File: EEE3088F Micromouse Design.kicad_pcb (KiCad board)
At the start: 2 copper layers, 74.5 x 78.2 mm, 62 parts, among them J1 Conn_02x16_Odd_Even, J2 Conn_01x02, Q2 AO3400A, U1 INA219AxD, U11 DRV8833PW, U12 DRV8833PW, U13 AP22966DC8-7, U15 TP4056-42-ESOP8, U6 TPS5430DDA, U9 CH224K

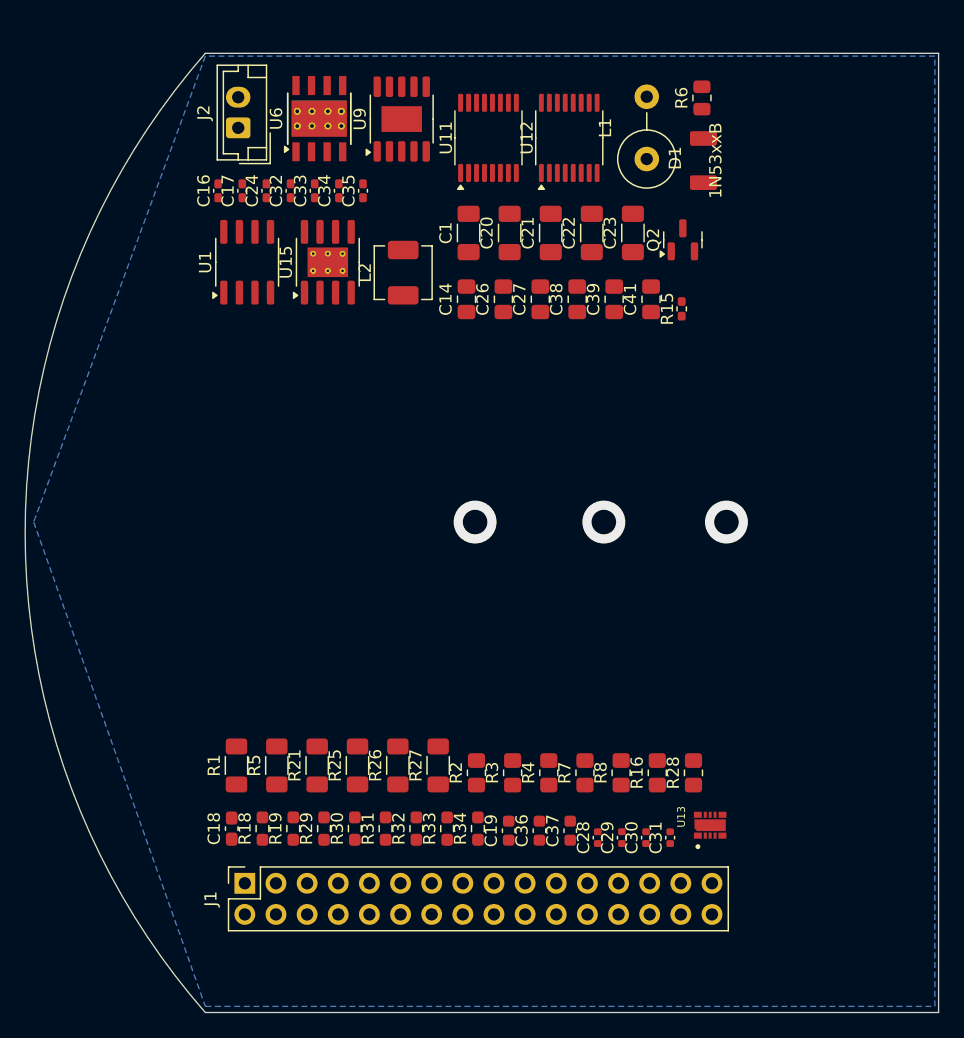
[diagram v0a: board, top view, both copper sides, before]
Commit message: Please Read: Replaced buck converter, removed old ones but this has left behind a gap in the copper. The board also needs a curved arc according to Justin. Still need footprints for key ICs, connectors and my switch
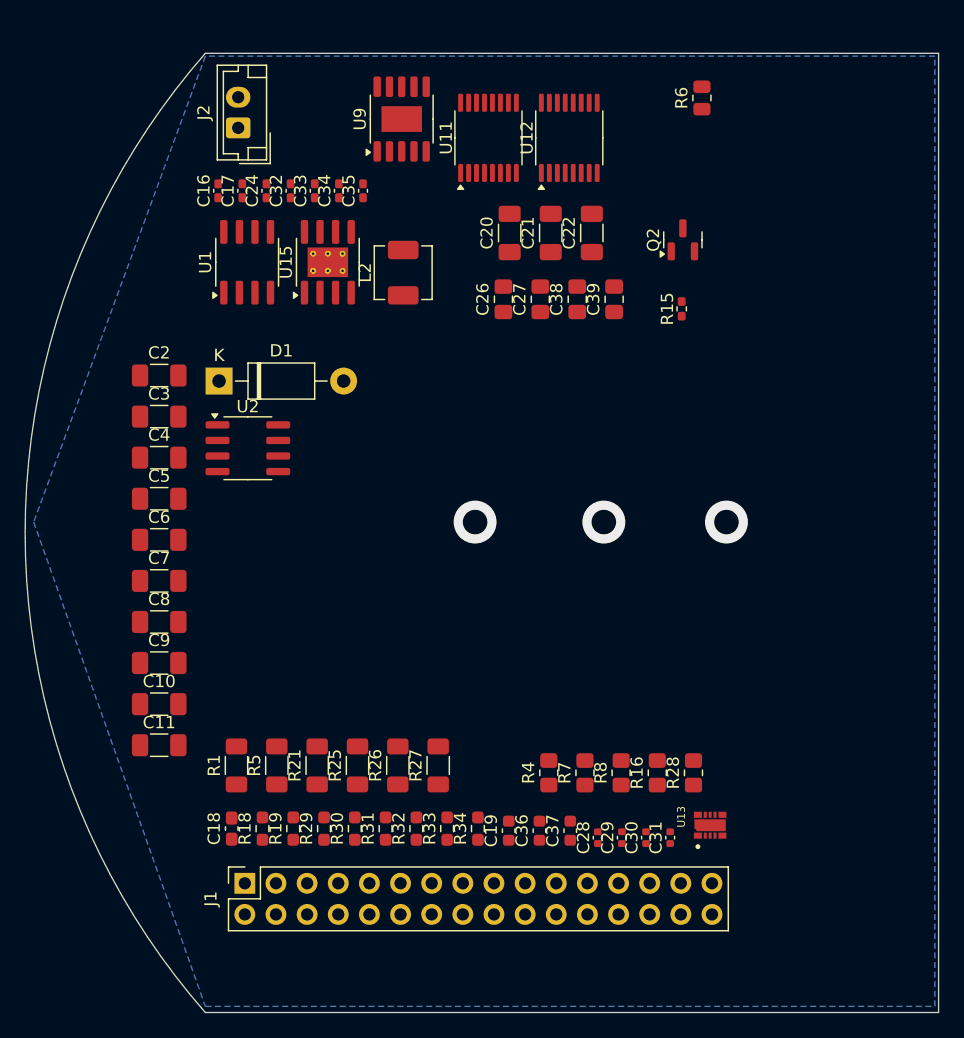
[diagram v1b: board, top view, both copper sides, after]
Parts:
- removed C1, C23: 100uF, Capacitor_SMD:C_1206_3216Metric_Pad1.33x1.80mm_HandSolder
- removed C14: 0.01uF, Capacitor_SMD:C_0805_2012Metric_Pad1.18x1.45mm_HandSolder
- removed C41: 47uF, Capacitor_SMD:C_0805_2012Metric_Pad1.18x1.45mm_HandSolder
- removed L1: 20uH, Inductor_THT:L_Axial_L11.0mm_D4.5mm_P5.08mm_Vertical_Fastron_MECC
- removed R2: 5.6k, Resistor_SMD:R_0805_2012Metric_Pad1.20x1.40mm_HandSolder
- removed R3: 3.3k, Resistor_SMD:R_0805_2012Metric_Pad1.20x1.40mm_HandSolder
- removed U6: TPS5430DDA, Package_SO:TI_SO-PowerPAD-8_ThermalVias
- added C10: 47uF, Capacitor_SMD:C_1206_3216Metric_Pad1.33x1.80mm_HandSolder, F.Cu at (50.7, 109.8)
- added C11: 47uF, Capacitor_SMD:C_1206_3216Metric_Pad1.33x1.80mm_HandSolder, F.Cu at (50.7, 113.2)
- added C2: 100uF, Capacitor_SMD:C_1206_3216Metric_Pad1.33x1.80mm_HandSolder, F.Cu at (50.7, 83.0)
- added C3: 100uF, Capacitor_SMD:C_1206_3216Metric_Pad1.33x1.80mm_HandSolder, F.Cu at (50.7, 86.4)
- added C4: 100uF, Capacitor_SMD:C_1206_3216Metric_Pad1.33x1.80mm_HandSolder, F.Cu at (50.7, 89.8)
- added C5: 100uF, Capacitor_SMD:C_1206_3216Metric_Pad1.33x1.80mm_HandSolder, F.Cu at (50.7, 93.1)
- added C6: 100uF, Capacitor_SMD:C_1206_3216Metric_Pad1.33x1.80mm_HandSolder, F.Cu at (50.7, 96.5)
- added C7: 47uF, Capacitor_SMD:C_1206_3216Metric_Pad1.33x1.80mm_HandSolder, F.Cu at (50.7, 99.8)
- added C8: 100uF, Capacitor_SMD:C_1206_3216Metric_Pad1.33x1.80mm_HandSolder, F.Cu at (50.7, 103.2)
- added C9: 100uF, Capacitor_SMD:C_1206_3216Metric_Pad1.33x1.80mm_HandSolder, F.Cu at (50.7, 106.5)
- added U2: XL1509-3.3, Package_SO:SOIC-8_3.9x4.9mm_P1.27mm, F.Cu at (58.0, 89.0)
- D1: value 1N53xxB -> 1N5819; footprint Inductor_1.2uH:L_custom_SMD -> Diode_THT:D_DO-41_SOD81_P10.16mm_Horizontal
- moved D1 43.4 mm to (55.6, 83.5), turned to 0 degrees

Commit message: Added footprints for inductors and tantalum capacitors. Also merged buck back to charging IC, and added test points
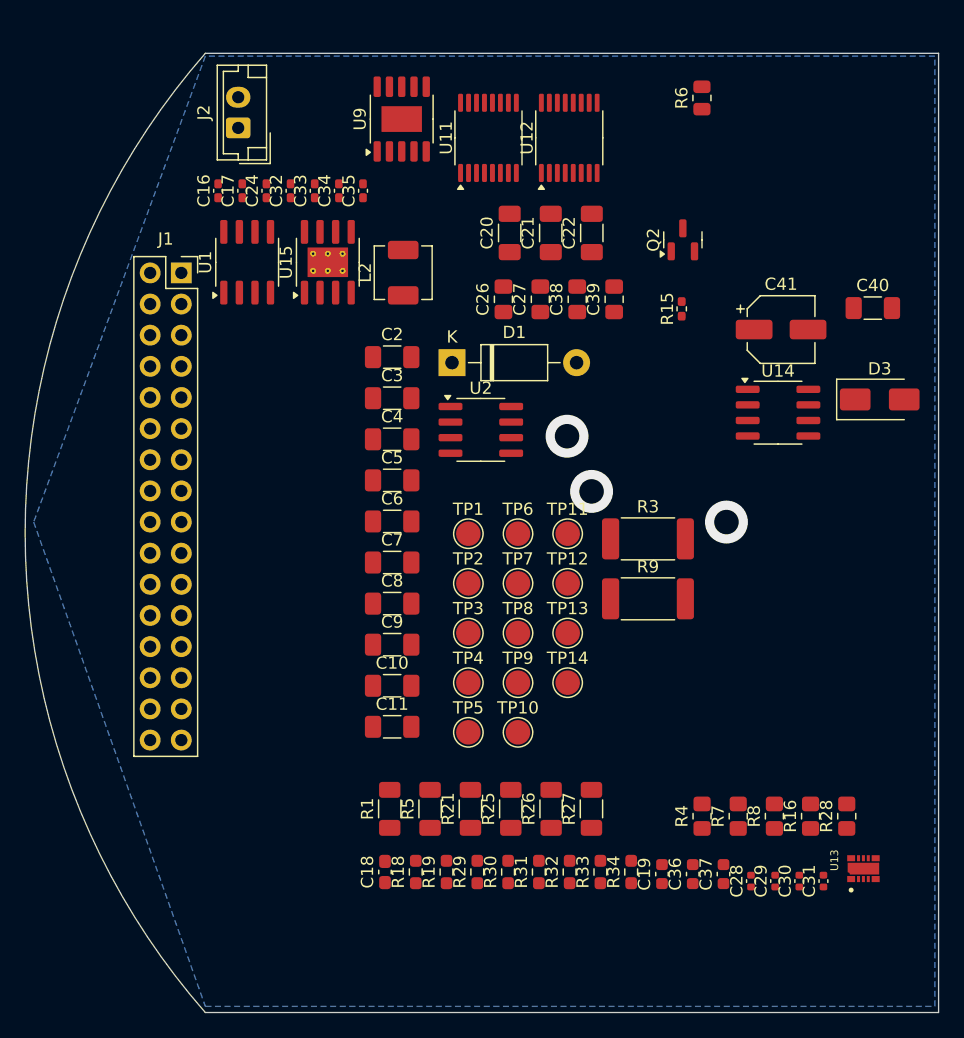
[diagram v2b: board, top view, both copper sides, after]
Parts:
- added C40: 100μF, Capacitor_SMD:C_1206_3216Metric_Pad1.33x1.80mm_HandSolder, F.Cu at (108.9, 77.5)
- added C41: 180uF 35V, Capacitor_SMD:CP_Elec_5x3, F.Cu at (101.5, 79.3)
- added D3: SS32, Diode_SMD:D_SMA, F.Cu at (109.5, 85.0)
- added R3: 2, Resistor_SMD:R_2512_6332Metric_Pad1.40x3.35mm_HandSolder, F.Cu at (90.6, 96.4)
- added R9: 2, Resistor_SMD:R_2512_6332Metric_Pad1.40x3.35mm_HandSolder, F.Cu at (90.6, 101.3)
- added TP1: TestPoint, TestPoint:TestPoint_Pad_D2.0mm, F.Cu at (76.0, 96.0)
- added TP10: TestPoint, TestPoint:TestPoint_Pad_D2.0mm, F.Cu at (80.0, 112.2)
- added TP11: TestPoint, TestPoint:TestPoint_Pad_D2.0mm, F.Cu at (84.0, 96.0)
- added TP12: TestPoint, TestPoint:TestPoint_Pad_D2.0mm, F.Cu at (84.0, 100.0)
- added TP13: TestPoint, TestPoint:TestPoint_Pad_D2.0mm, F.Cu at (84.0, 104.0)
- added TP14: TestPoint, TestPoint:TestPoint_Pad_D2.0mm, F.Cu at (84.0, 108.1)
- added TP2: TestPoint, TestPoint:TestPoint_Pad_D2.0mm, F.Cu at (76.0, 100.0)
- added TP3: TestPoint, TestPoint:TestPoint_Pad_D2.0mm, F.Cu at (76.0, 104.0)
- added TP4: TestPoint, TestPoint:TestPoint_Pad_D2.0mm, F.Cu at (76.0, 108.1)
- added TP5: TestPoint, TestPoint:TestPoint_Pad_D2.0mm, F.Cu at (76.0, 112.2)
- added TP6: TestPoint, TestPoint:TestPoint_Pad_D2.0mm, F.Cu at (80.0, 96.0)
- added TP7: TestPoint, TestPoint:TestPoint_Pad_D2.0mm, F.Cu at (80.0, 100.0)
- added TP8: TestPoint, TestPoint:TestPoint_Pad_D2.0mm, F.Cu at (80.0, 104.0)
- added TP9: TestPoint, TestPoint:TestPoint_Pad_D2.0mm, F.Cu at (80.0, 108.1)
- added U14: XL1509-5.0, Package_SO:SOIC-8_3.9x4.9mm_P1.27mm, F.Cu at (101.2, 86.1)
- C28, C30: value 2.2uF -> 10nF
- moved J1 50.0 mm to (52.5, 74.7), turned to 0 degrees
- moved D1 19.1 mm to (74.6, 82.0)
- moved C10 19.1 mm to (69.7, 108.3)
- moved C11 19.1 mm to (69.7, 111.7)
- moved C2 19.1 mm to (69.7, 81.5)
- moved C3 19.1 mm to (69.7, 84.9)
- moved C4 19.1 mm to (69.7, 88.2)
- moved C5 19.1 mm to (69.7, 91.6)
- moved C6 19.1 mm to (69.7, 95.0)
- moved C7 19.1 mm to (69.7, 98.3)
- moved C8 19.1 mm to (69.7, 101.7)
- moved C9 19.1 mm to (69.7, 105.0)
- moved U2 19.1 mm to (77.0, 87.5)
- moved C18 13.0 mm to (69.2, 123.5)
- moved R1 13.0 mm to (69.5, 118.4)
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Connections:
- C26 pad 1: /V_Battery+ -> GND
- C26 pad 2: Net-(U12-VM) -> /V_Battery+
- C28 pad 1: Net-(U11-VM) -> /V_Battery+
- C30 pad 1: Net-(U12-VM) -> /V_Battery+
- C38 pad 1: /V_Battery+ -> GND
- C38 pad 2: Net-(U11-VM) -> /V_Battery+
- U11 pad 12: Net-(U11-VM) -> /V_Battery+
- U12 pad 12: Net-(U12-VM) -> /V_Battery+
- U15 pad 4: /HV -> Net-(U15-CE)
- U15 pad 8: /HV -> Net-(U15-CE)

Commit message: Added footprints for inductor, switch and type-c connector
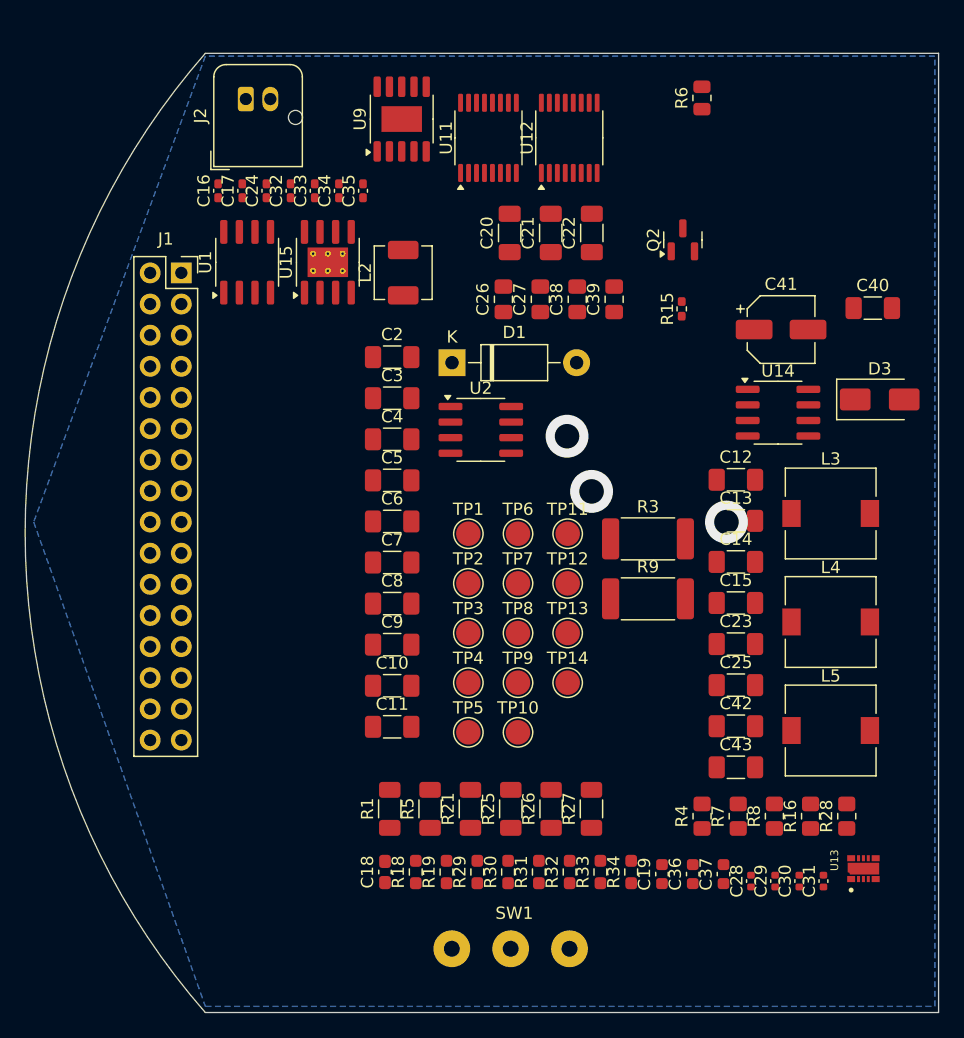
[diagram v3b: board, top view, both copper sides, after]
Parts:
- added C12: 100uF, Capacitor_SMD:C_1206_3216Metric_Pad1.33x1.80mm_HandSolder, F.Cu at (97.8, 91.5)
- added C13: 100uF, Capacitor_SMD:C_1206_3216Metric_Pad1.33x1.80mm_HandSolder, F.Cu at (97.8, 94.9)
- added C14: 47uF, Capacitor_SMD:C_1206_3216Metric_Pad1.33x1.80mm_HandSolder, F.Cu at (97.8, 98.2)
- added C15: 47uF, Capacitor_SMD:C_1206_3216Metric_Pad1.33x1.80mm_HandSolder, F.Cu at (97.8, 101.6)
- added C23: 100uF, Capacitor_SMD:C_1206_3216Metric_Pad1.33x1.80mm_HandSolder, F.Cu at (97.8, 105.0)
- added C25: 100uF, Capacitor_SMD:C_1206_3216Metric_Pad1.33x1.80mm_HandSolder, F.Cu at (97.8, 108.3)
- added C42: 47uF, Capacitor_SMD:C_1206_3216Metric_Pad1.33x1.80mm_HandSolder, F.Cu at (97.8, 111.7)
- added C43: 47uF, Capacitor_SMD:C_1206_3216Metric_Pad1.33x1.80mm_HandSolder, F.Cu at (97.8, 115.0)
- added L3: 22uH, Inductor_SMD:L_7.3x7.3_H4.5, F.Cu at (105.5, 94.3)
- added L4: 22uH, Inductor_SMD:L_7.3x7.3_H4.5, F.Cu at (105.5, 103.2)
- added L5: 22uH, Inductor_SMD:L_7.3x7.3_H4.5, F.Cu at (105.5, 112.0)
- added SW1: SW_SPDT, HX_SS12D10G6_Switch:Untitled, F.Cu at (79.4, 129.8)
- J2: footprint Connector_JST:JST_EH_B2B-EH-A_1x02_P2.50mm_Vertical -> Connector_JST:JST_JWPF_B02B-JWPF-SK-R_1x02_P2.00mm_Vertical
- moved J2 2.43 mm to (57.8, 60.5)
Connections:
- R9 pad 2: Net-(U15-CE) -> unconnected-(R9-Pad2)
- TP10 pad 1: Net-(U15-CE) -> /Stepped Down 5V
- U14 pad 3: Net-(U14-FB) -> /Stepped Down 5V
- U15 pad 4: Net-(U15-CE) -> /Stepped Down 5V
- U15 pad 8: Net-(U15-CE) -> /Stepped Down 5V

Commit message: Fixed the arc to match spec. Added Daniel's components and added all LCSC numbers for them. Fixed the connector footprint, although JST one still needs to be corrected
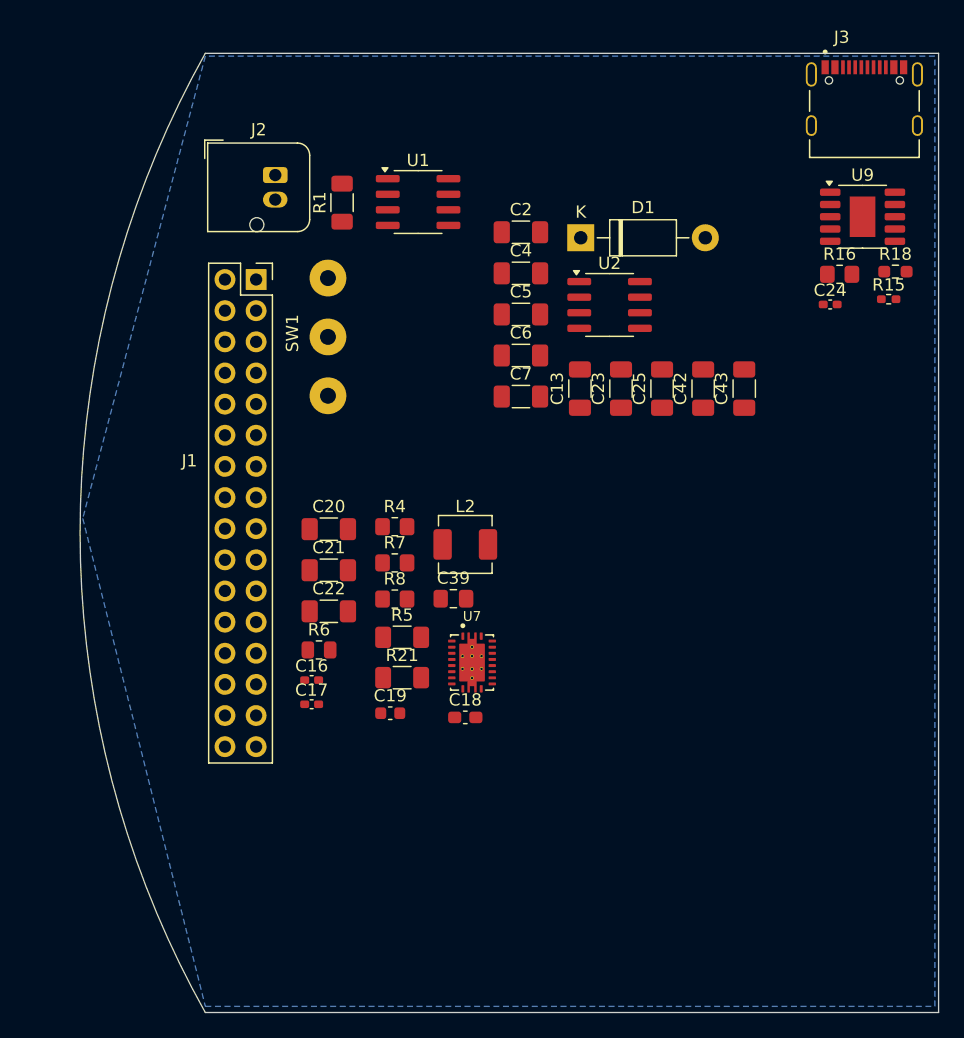
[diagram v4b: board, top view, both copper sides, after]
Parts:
- removed C10, C11, C14, C15: 47uF, Capacitor_SMD:C_1206_3216Metric_Pad1.33x1.80mm_HandSolder
- removed C12, C3, C8, C9: 100uF, Capacitor_SMD:C_1206_3216Metric_Pad1.33x1.80mm_HandSolder
- removed C26, C27, C38: 10uF, Capacitor_SMD:C_0805_2012Metric_Pad1.18x1.45mm_HandSolder
- removed C28, C30: 10nF, Capacitor_SMD:C_0402_1005Metric
- removed C29, C31: 2.2uF, Capacitor_SMD:C_0402_1005Metric
- removed C32, C33, C34, C35: 1uF, Capacitor_SMD:C_0402_1005Metric_Pad0.74x0.62mm_HandSolder
- removed C36, C37: 1nF, Capacitor_SMD:C_0603_1608Metric
- removed C40: 100μF, Capacitor_SMD:C_1206_3216Metric_Pad1.33x1.80mm_HandSolder
- removed C41: 180uF 35V, Capacitor_SMD:CP_Elec_5x3
- removed D3: SS32, Diode_SMD:D_SMA
- removed L3, L4, L5: 22uH, Inductor_SMD:L_7.3x7.3_H4.5
- removed Q2: AO3400A, Package_TO_SOT_SMD:SOT-23
- removed R19: 10k, Resistor_SMD:R_0603_1608Metric_Pad0.98x0.95mm_HandSolder
- removed R25, R26: 1, Resistor_SMD:R_1206_3216Metric_Pad1.30x1.75mm_HandSolder
- removed R27: 4.7k, Resistor_SMD:R_1206_3216Metric_Pad1.30x1.75mm_HandSolder
- removed R28: 330, Resistor_SMD:R_0805_2012Metric_Pad1.20x1.40mm_HandSolder
- removed R29, R30, R31, R32: 0.82, Resistor_SMD:R_0603_1608Metric_Pad0.98x0.95mm_HandSolder
- removed R3, R9: 2, Resistor_SMD:R_2512_6332Metric_Pad1.40x3.35mm_HandSolder
- removed R33: 2.2k, Resistor_SMD:R_0603_1608Metric_Pad0.98x0.95mm_HandSolder
- removed R34: 270, Resistor_SMD:R_0603_1608Metric_Pad0.98x0.95mm_HandSolder
- removed TP1, TP10, TP11, TP12, TP13, TP14, TP2, TP3, TP4, TP5, TP6, TP7, TP8, TP9: TestPoint, TestPoint:TestPoint_Pad_D2.0mm
- removed U11, U12: DRV8833PW, Package_SO:TSSOP-16_4.4x5mm_P0.65mm
- removed U13: AP22966DC8-7, AP22966DC8-7:IC_AP22966DC8-7
- removed U14: XL1509-5.0, Package_SO:SOIC-8_3.9x4.9mm_P1.27mm
- removed U15: TP4056-42-ESOP8, Package_SO:SOIC-8-1EP_3.9x4.9mm_P1.27mm_EP2.41x3.3mm_ThermalVias
- added J3: TYPE-C-31-M-12, Footprints:HRO_TYPE-C-31-M-12, F.Cu at (108.2, 62.7)
- added U7: TPS61088RHLR, TPS61088:IC_TPS61088RHLR, F.Cu at (76.2, 106.5)
- moved R18 62.7 mm to (110.8, 74.6), turned to 0 degrees
- moved R6 54.8 mm to (63.8, 105.4), turned to 0 degrees
- moved SW1 52.1 mm to (64.5, 79.9), turned to 90 degrees
- moved R1 49.6 mm to (65.7, 69.0)
- moved C24 46.9 mm to (105.5, 77.3), turned to 0 degrees
- moved R16 44.3 mm to (106.2, 74.8), turned to 0 degrees
- moved C17 42.3 mm to (63.2, 109.9), turned to 0 degrees
- moved C16 40.6 mm to (63.2, 107.9), turned to 0 degrees
- moved U9 38.4 mm to (108.1, 70.1), turned to 0 degrees
- moved C22 37.6 mm to (64.6, 102.3), turned to 0 degrees
- moved R8 35.7 mm to (70.0, 101.3), turned to 0 degrees
- moved R7 34.8 mm to (70.0, 98.3), turned to 0 degrees
- moved R4 34.4 mm to (70.0, 95.4), turned to 0 degrees
- moved C21 32.9 mm to (64.6, 98.9), turned to 0 degrees
- moved C43 30.9 mm to (98.5, 84.1), turned to 90 degrees
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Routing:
- net GND: vias 3 -> 0
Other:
- board size 74.5 x 78.2 mm -> 70 x 78.2 mm
